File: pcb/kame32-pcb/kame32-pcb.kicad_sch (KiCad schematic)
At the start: 11 parts, among them J2 Conn_02x04_Odd_Even, J3 Conn_01x04, J4 Conn_01x04, J5 Conn_01x02, J6 Conn_02x04_Odd_Even, SW1 SW_SPDT, U1 TEA1-0505

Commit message: PCB before DCDC change
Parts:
- added J1: Conn_01x06, Connector_PinHeader_2.54mm:PinHeader_1x06_P2.54mm_Vertical, symbol Connector_Generic:Conn_01x06
- added J7: Conn_01x05, Connector_PinHeader_2.54mm:PinHeader_1x05_P2.54mm_Vertical, symbol Connector_Generic:Conn_01x05
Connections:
- net +8V: now also J1.1 (Pin_1)
- net -BATT: now also J1.2 (Pin_2)
- net at J3.1 (Pin_1): now also U2.26 (D21); no longer U2.3 (D13)
- net at J3.2 (Pin_2): now also U2.25 (D19); no longer U2.4 (D12)
- net at J3.3 (Pin_3): now also U2.24 (D18); no longer U2.5 (D14)
- net at J3.4 (Pin_4): now also U2.23 (D5); no longer U2.6 (D27)
- net at U2.18 (D15): now also J7.5 (Pin_5)
- net at U2.19 (D2): now also J7.4 (Pin_4)
- net at U2.20 (D4): now also J7.3 (Pin_3)
- net at U2.21 (RX2): now also J7.2 (Pin_2)
- net at U2.22 (TX2): now also J7.1 (Pin_1)
- new net: J1.3 (Pin_3), U2.3 (D13)
- new net: J1.4 (Pin_4), U2.4 (D12)
- new net: J1.5 (Pin_5), U2.5 (D14)
- new net: J1.6 (Pin_6), U2.6 (D27)
- no-connect marks 19 -> 8
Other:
- moved on the sheet: J3

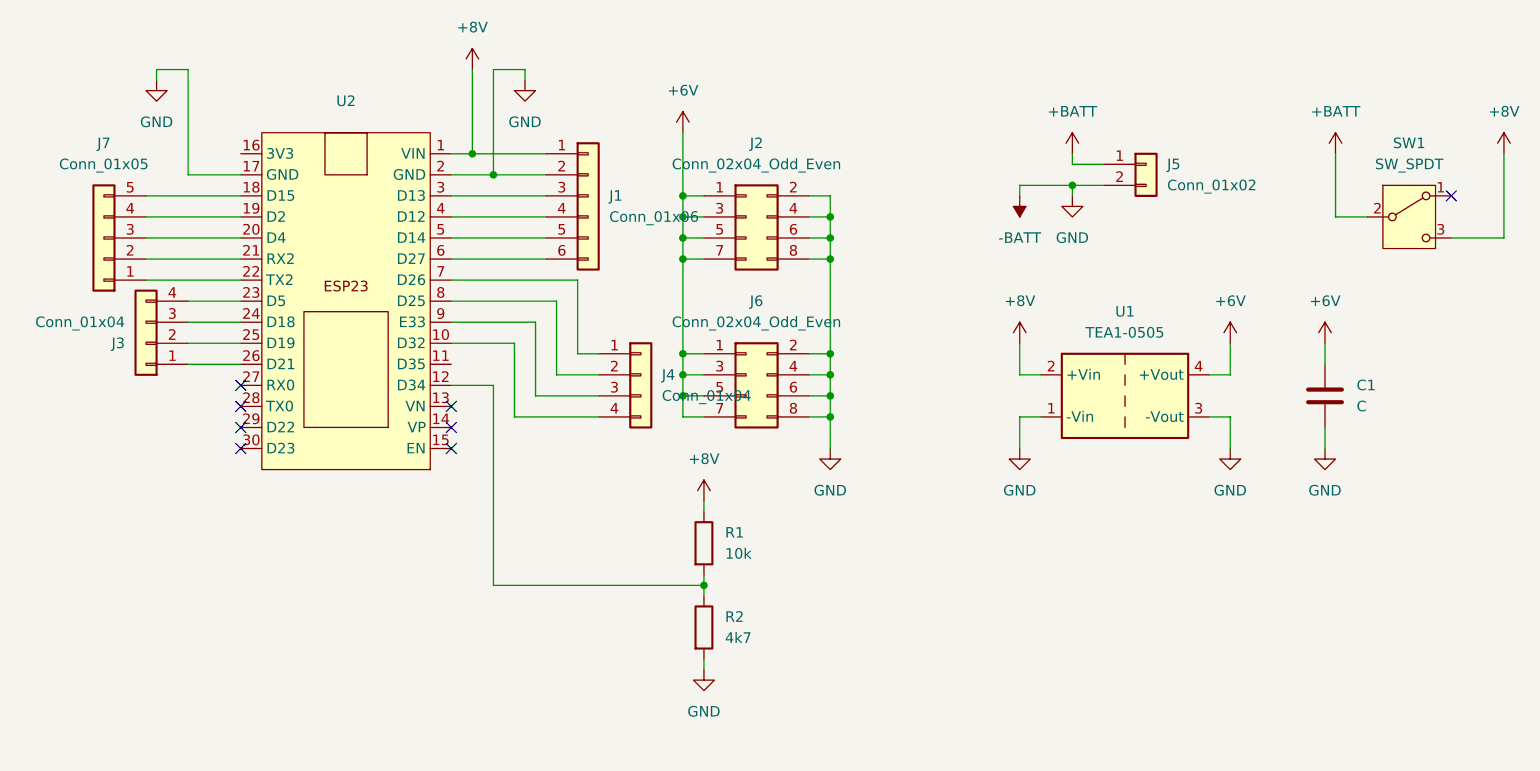
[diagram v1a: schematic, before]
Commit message: esp32 pcb with servo headers
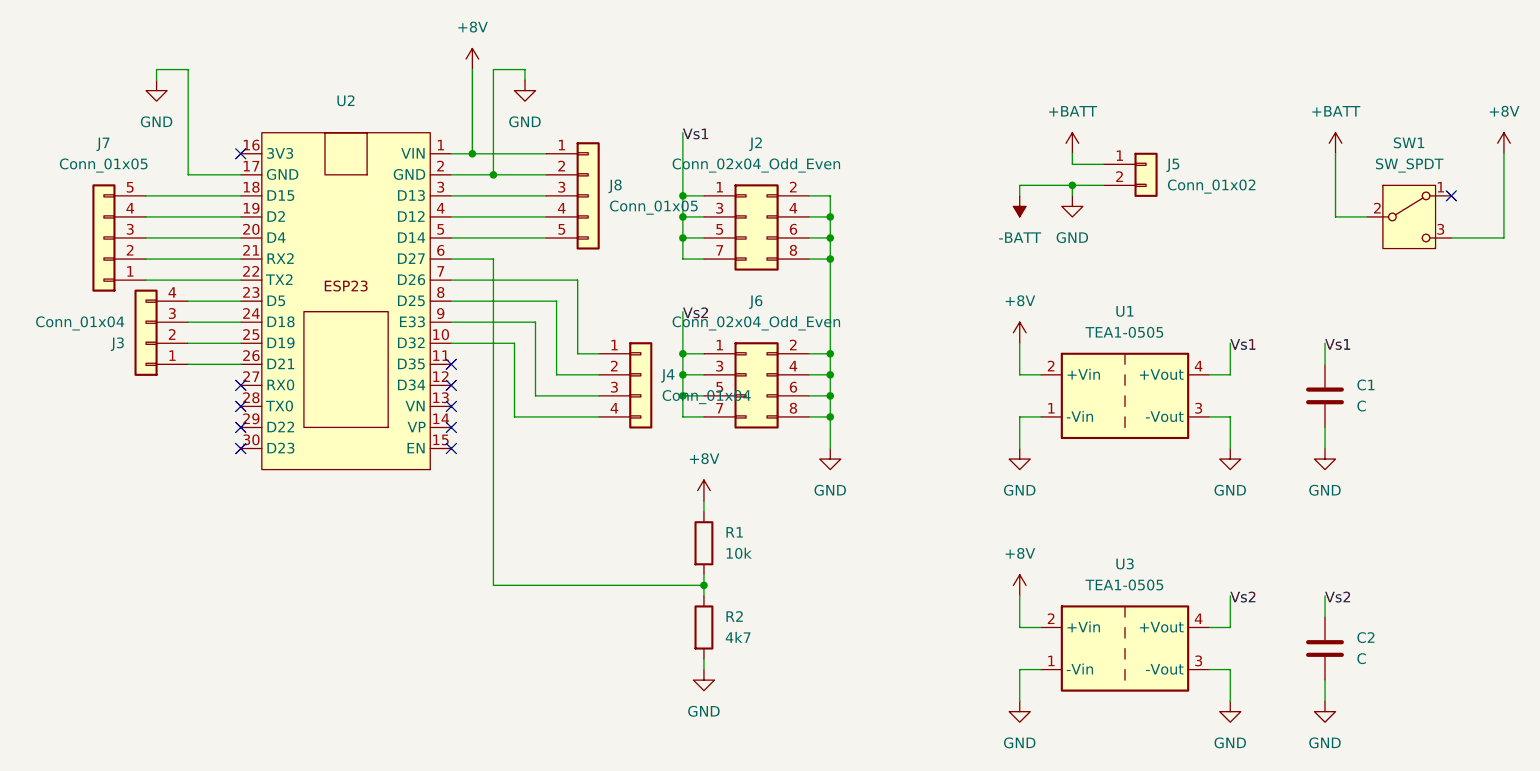
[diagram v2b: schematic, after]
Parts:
- removed J1: Conn_01x06, Connector_PinHeader_2.54mm:PinHeader_1x06_P2.54mm_Vertical, symbol Connector_Generic:Conn_01x06
- added C2: C, Capacitor_THT:CP_Radial_D5.0mm_P2.50mm, symbol Device:C
- added J8: Conn_01x05, Connector_PinHeader_2.54mm:PinHeader_1x05_P2.54mm_Vertical, symbol Connector_Generic:Conn_01x05
- added U3: TEA1-0505, kame32:dcdc, symbol Converter_DCDC:TEA1-0505
- U1: footprint Connector_PinHeader_2.54mm:PinHeader_2x02_P2.54mm_Vertical -> kame32:dcdc
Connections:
- net +8V: now also J8.1 (Pin_1), U3.2 (+Vin)
- net -BATT: now also C2.2, J8.2 (Pin_2), U3.1 (-Vin), U3.3 (-Vout)
- net at U2.3 (D13): now also J8.3 (Pin_3)
- net at U2.4 (D12): now also J8.4 (Pin_4)
- net at U2.5 (D14): now also J8.5 (Pin_5)
- net at U2.6 (D27): now also R1.2, R2.1
- net +6V renamed Vs1
- net Vs1: no longer J6.1 (Pin_1), J6.3 (Pin_3), J6.5 (Pin_5), J6.7 (Pin_7)
- new net Vs2: C2.1, J6.1 (Pin_1), J6.3 (Pin_3), J6.5 (Pin_5), J6.7 (Pin_7), U3.4 (+Vout)
- now unconnected: U2.12 (D34)
- no-connect marks 8 -> 11
